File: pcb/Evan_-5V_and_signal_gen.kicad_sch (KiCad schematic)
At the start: 28 parts, among them IC1 TL7660IDGKR, IC2 TL081IDT, IC4 UA78M33CDCYG3, J2 M22-6003005, U5 TPS2069CDBVR_MOSFET

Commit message: connect mcu 3.3vreg to +5v_ext so it always has power
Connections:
- net +5V: no longer C25.1, IC4.1 (INPUT)
- net +5V_EXT: now also C25.1, IC4.1 (INPUT)
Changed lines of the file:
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@@
   (junction (at 207.01 86.868) (diameter 0) (color 0 0 0 0)
+  )
+  (junction (at 62.23 124.714) (diameter 0) (color 0 0 0 0)
   )
   (junction (at 262.89 105.41) (diameter 0) (color 0 0 0 0)
@@
     (stroke (width 0) (type default))
   )
+  (wire (pts (xy 29.718 83.82) (xy 29.718 124.714))
+    (stroke (width 0) (type default))
+  )
   (wire (pts (xy 44.45 158.75) (xy 44.45 161.29))
     (stroke (width 0) (type default))
@@
     (stroke (width 0) (type default))
   )
+  (wire (pts (xy 29.718 83.82) (xy 49.53 83.82))
+    (stroke (width 0) (type default))
+  )
   (wire (pts (xy 95.25 35.56) (xy 73.66 35.56))
     (stroke (width 0) (type default))
@@
     (stroke (width 0) (type default))
   )
+  (wire (pts (xy 62.23 124.714) (xy 29.718 124.714))
+    (stroke (width 0) (type default))
+  )
   (wire (pts (xy 95.25 33.02) (xy 95.25 35.56))
     (stroke (width 0) (type default))
@@
     (stroke (width 0) (type default))
   )
+  (wire (pts (xy 62.23 124.714) (xy 62.23 133.35))
+    (stroke (width 0) (type default))
+  )
   (wire (pts (xy 15.24 41.91) (xy 35.56 41.91))
     (stroke (width 0) (type default))
@@
     (stroke (width 0) (type default))
   )
-  (wire (pts (xy 27.94 83.82) (xy 49.53 83.82))
-    (stroke (width 0) (type default))
-  )
   (wire (pts (xy 63.5 92.71) (xy 77.47 92.71))
     (stroke (width 0) (type default))
@@
     (stroke (width 0) (type default))
   )
-  (wire (pts (xy 62.23 124.46) (xy 62.23 133.35))
+  (wire (pts (xy 62.23 124.46) (xy 62.23 124.714))
     (stroke (width 0) (type default))
   )
@@
         )
       )
-    )
-  )
-  (symbol (lib_id "power:+5V") (at 27.94 83.82 90) (unit 1)
-    (in_bom yes) (on_board yes) (dnp no) (fields_autoplaced)
-    (property "Reference" "#PWR035" (at 31.75 83.82 0)
-      (effects (font (size 1.27 1.27)) hide)
-    )
-    (property "Value" "+5V" (at 24.13 83.82 90)
-      (effects (font (size 1.27 1.27)) (justify left))
-    )
-    (property "Footprint" "" (at 27.94 83.82 0)
-      (effects (font (size 1.27 1.27)) hide)
-    )
-    (property "Datasheet" "" (at 27.94 83.82 0)
-      (effects (font (size 1.27 1.27)) hide)
-    )
-    (pin "1")
-    (instances
-      (project "mcu_integration"
-        (path "/c0210bc3-f67f-47d8-a34e-f002a728adb2/39708197-8fe0-4b5c-ba49-65ed06982da9"
-          (reference "#PWR035") (unit 1)
-        )
-      )

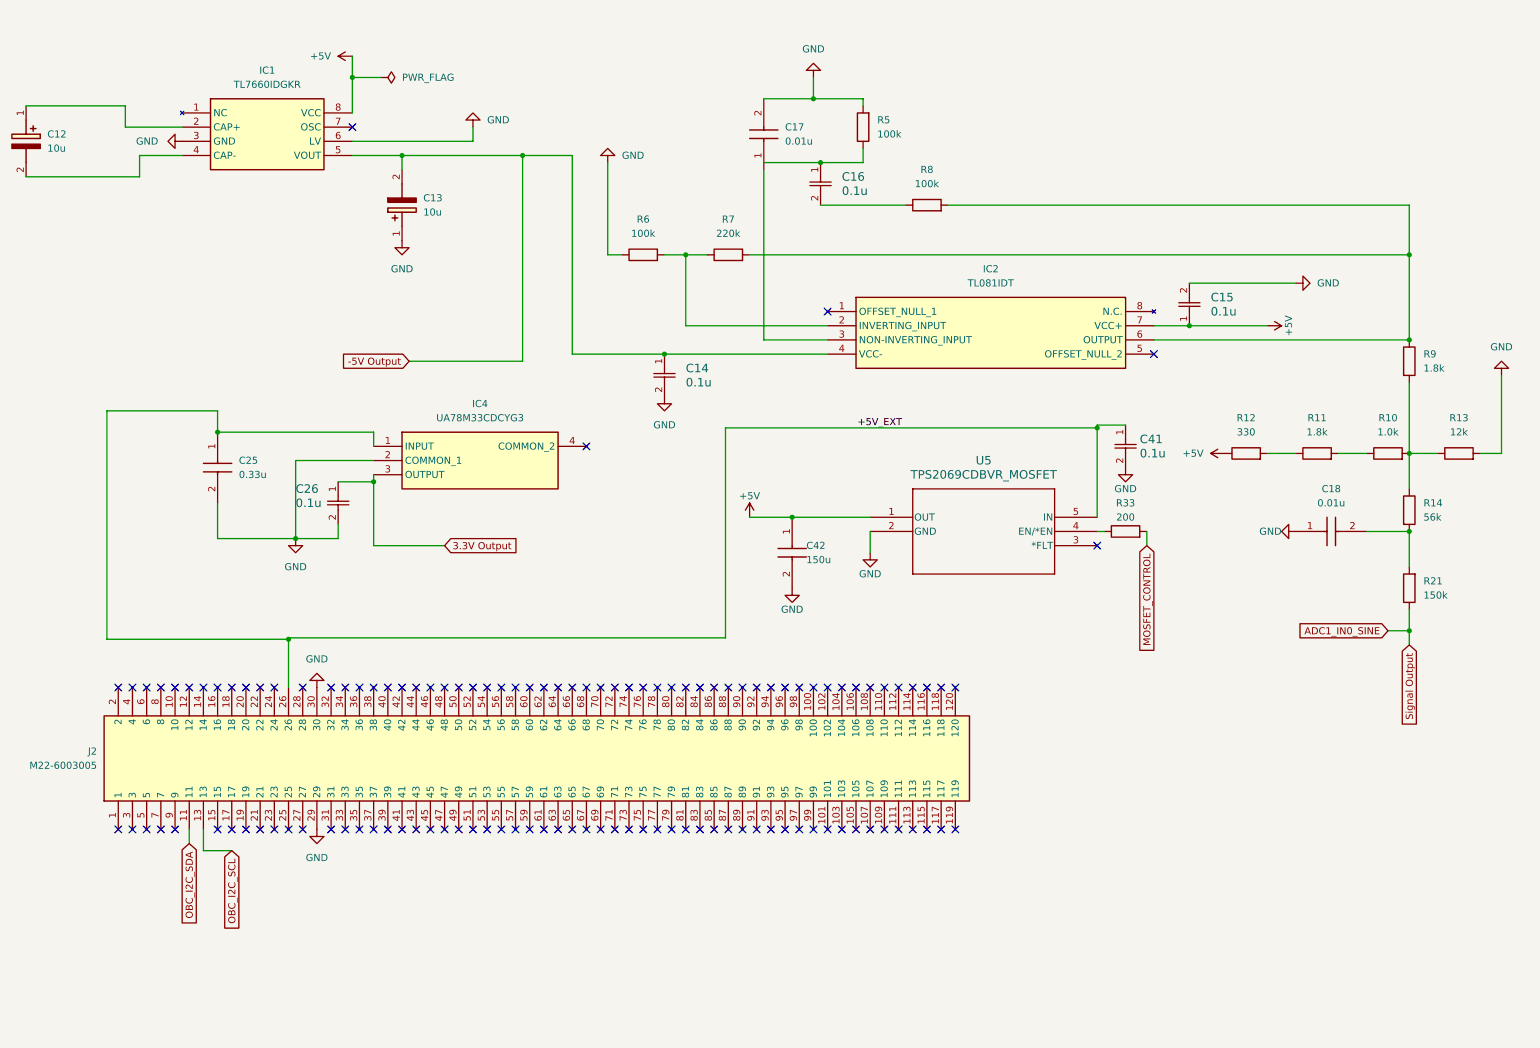
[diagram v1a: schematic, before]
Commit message: (accepted by jlc rev B) Karim rev2 cleanup (#18)
* fixed all errors and warnings, silk fixed

* add names to project

* misc cleanup

* TL766 footprint fixed

* proper holes added

* hole sizing done, evan cap fix

* mcu square wave sine header, more space for ic's should be ready for order

* ready for jlcpcb

* cleanup README

* close kicad before commit
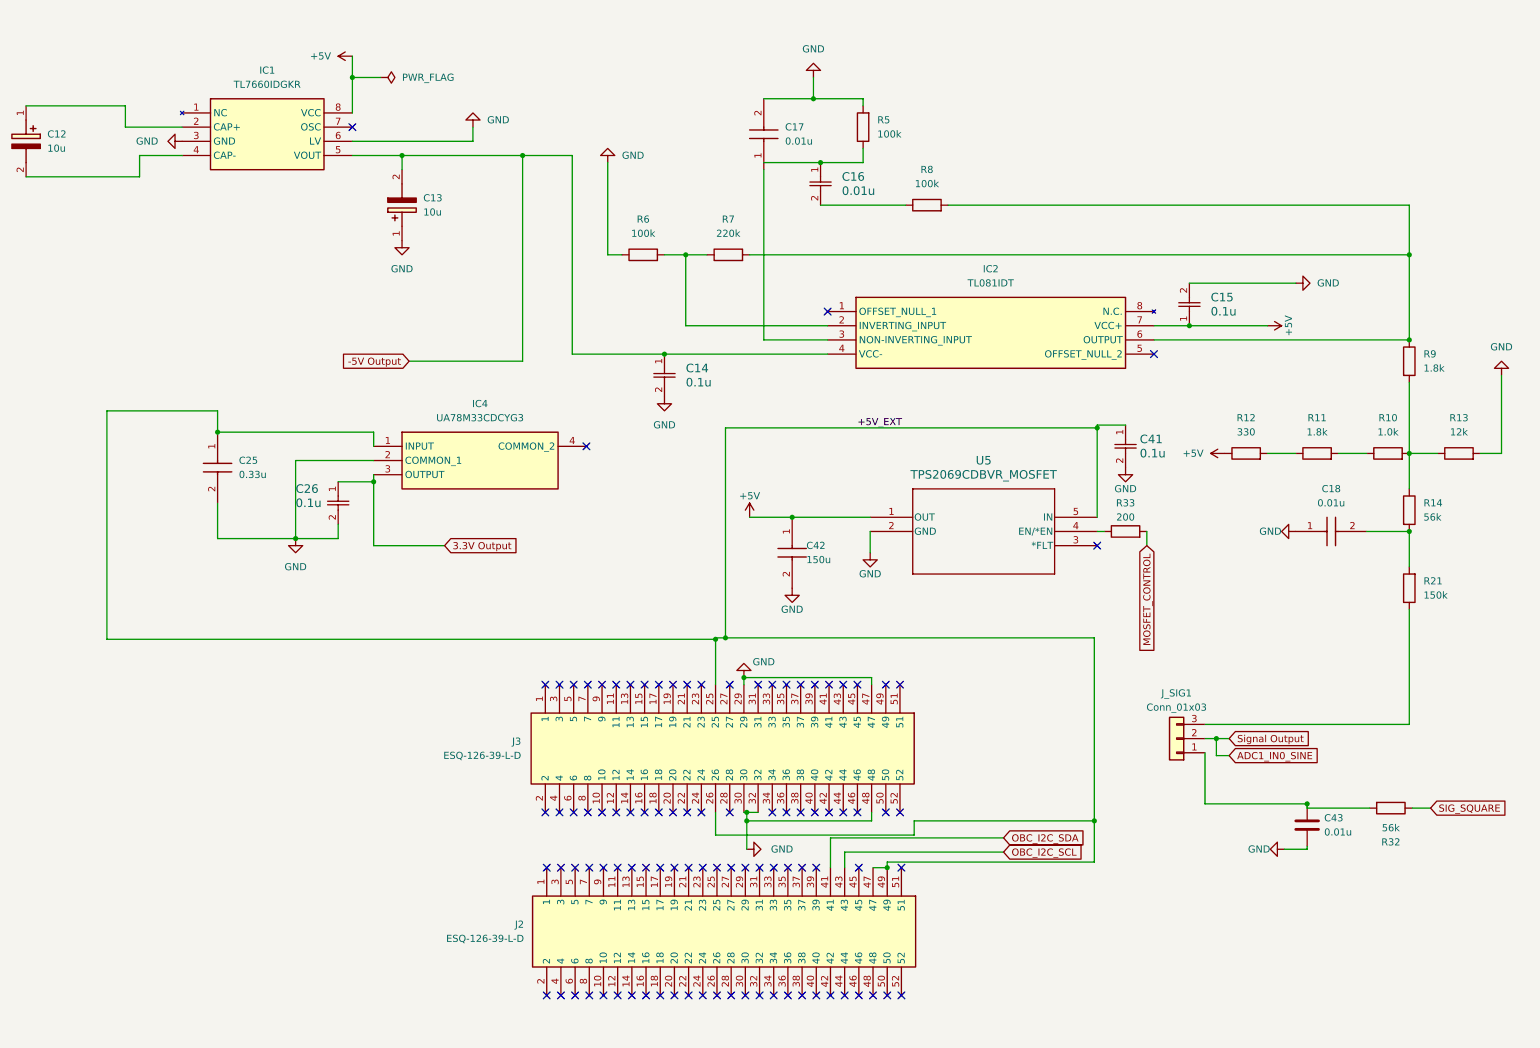
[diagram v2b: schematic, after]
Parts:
- removed J2: M22-6003005, capstone:RHDR120W55P200_4X30_6020X800X935P, symbol capstone:M22-6003005
- added C43: 0.01u, capstone:C0805, symbol Device:C
- added J2, J3: ESQ-126-39-L-D, capstone:ESQ-126-Y-X-D, symbol capstone:ESQ-126-39-L-D
- added J_SIG1: Conn_01x03, Connector_PinHeader_2.54mm:PinHeader_1x03_P2.54mm_Vertical, symbol Connector_Generic:Conn_01x03
- added R32: 56k, Resistor_SMD:R_0402_1005Metric, symbol Device:R
- C16: value 0.1u -> 0.01u
- IC1: footprint capstone:SOIC127P600X175-8N -> capstone:SOP65P490X110-8N-actual
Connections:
- net +5V_EXT: now also J2.47, J2.49, J3.25, J3.26
- net ADC1_IN0_SINE: now also J_SIG1.2 (Pin_2); no longer R21.1
- net GND: now also C43.1, J3.29, J3.30, J3.32, J3.47, J3.48
- net OBC_I2C_SCL: now also J2.43
- net OBC_I2C_SDA: now also J2.41
- new net: J_SIG1.3 (Pin_3), R21.1
- new net: C43.2, J_SIG1.1 (Pin_1), R32.2
- new net SIG_SQUARE: R32.1
- no-connect marks 120 -> 98

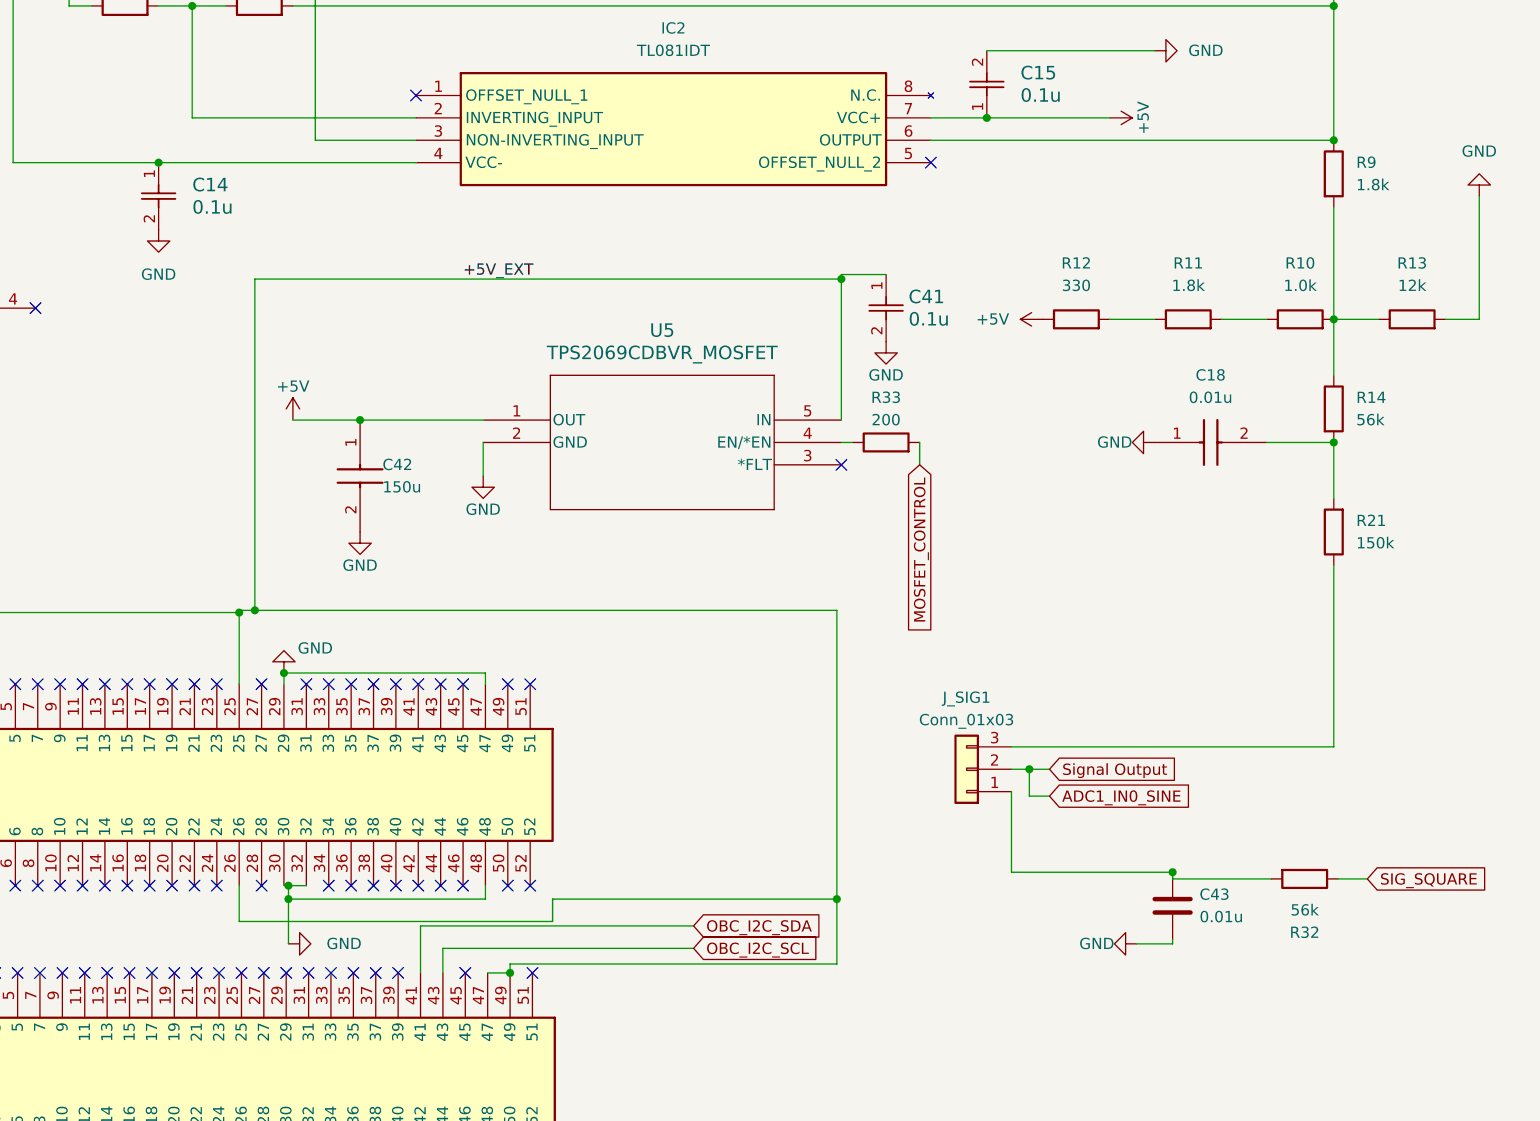
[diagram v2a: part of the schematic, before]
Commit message: Added-Voltage-follower-and-Changed-opto-resistor-values
Added the voltage follower circuit to the signal gen. Changed the R values on the optoisolator circuit.
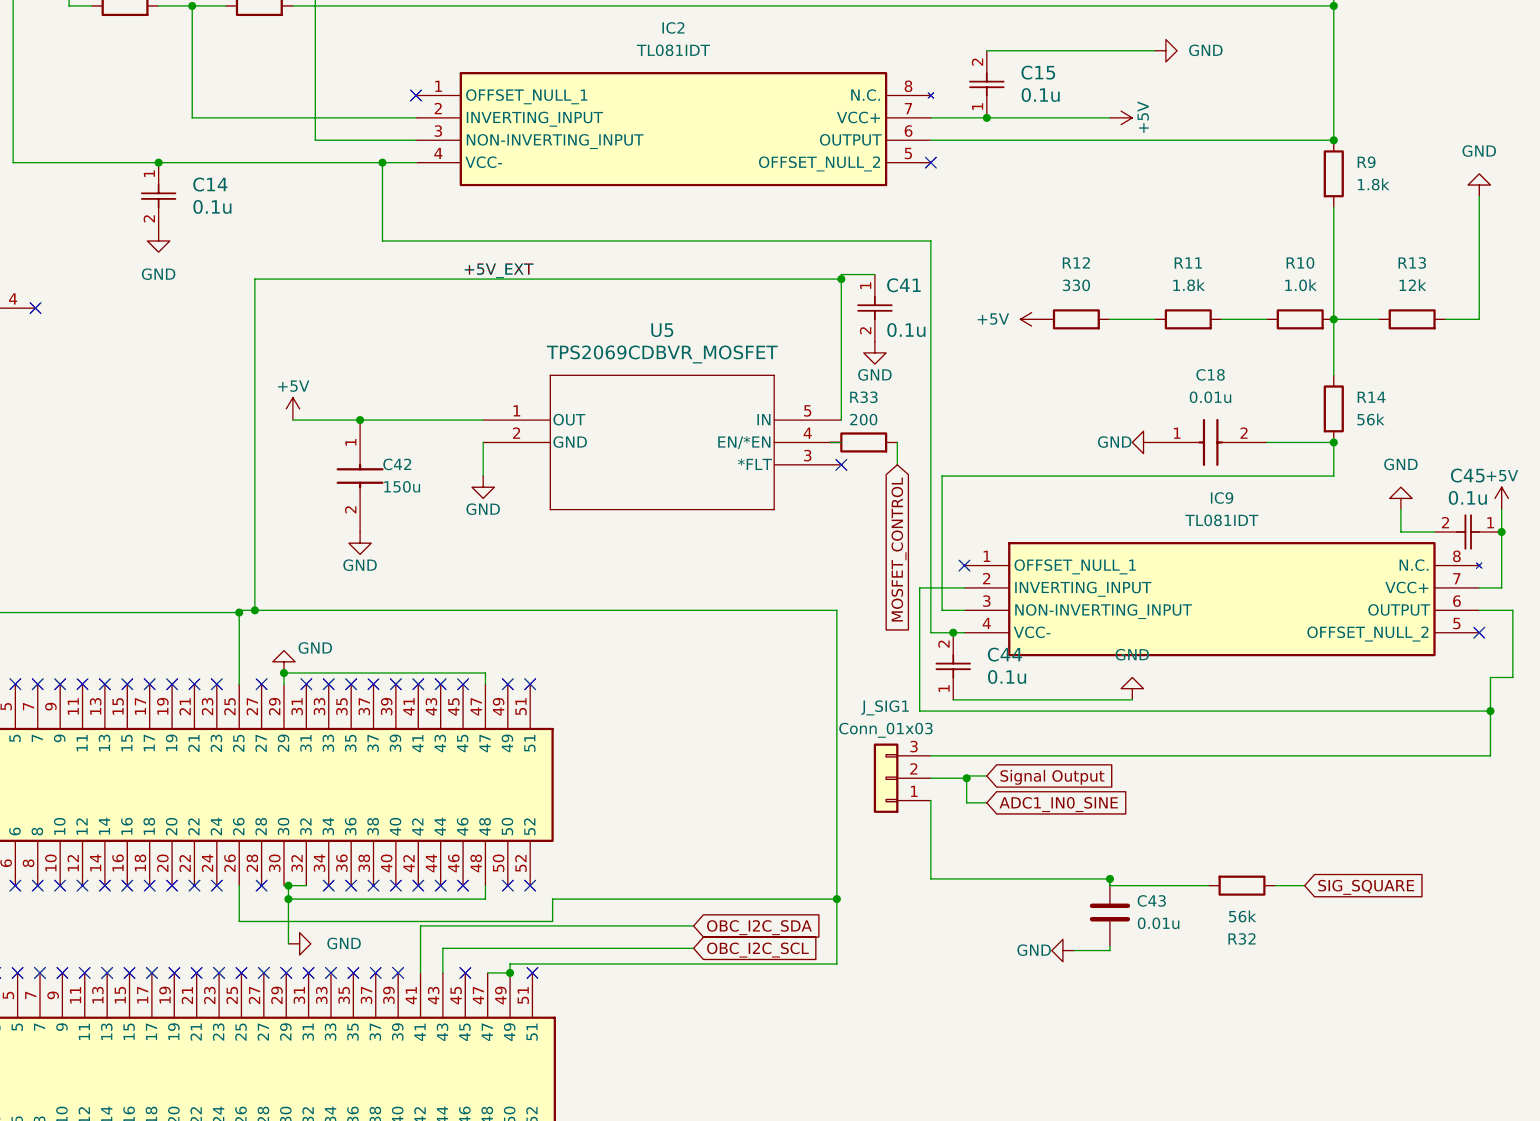
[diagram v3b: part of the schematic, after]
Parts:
- removed R21: 150k, Resistor_SMD:R_0402_1005Metric, symbol Device:R
- added C44, C45: 0.1u, capstone:CAPC220145_88N_KEM-0.1u, symbol capstone:C0805C104K5RAC7210
- added IC9: TL081IDT, capstone:SOIC127P600X175-8N, symbol capstone:TL081IDT
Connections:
- net +5V: now also C45.1, IC9.7 (VCC+)
- net -5V Output: now also C44.2, IC9.4 (VCC-)
- net GND: now also C44.1, C45.2
- net at J_SIG1.3 (Pin_3): now also IC9.2 (INVERTING_INPUT), IC9.6 (OUTPUT)
- net at C18.2, R14.2: now also IC9.3 (NON-INVERTING_INPUT)
- no-connect marks 98 -> 100
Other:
- moved on the sheet: C41, C43, J_SIG1, R32, R33
